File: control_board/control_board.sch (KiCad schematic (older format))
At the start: 38 parts, among them J1 Conn_01x08_Male, K1 G5Q-1A, Q1 Q_NPN_BEC, U1 MC78M05_TO252, U2 TSR_1-24120, U3 74LS02, U4 74LS02, U5 Conn_01x08_Male

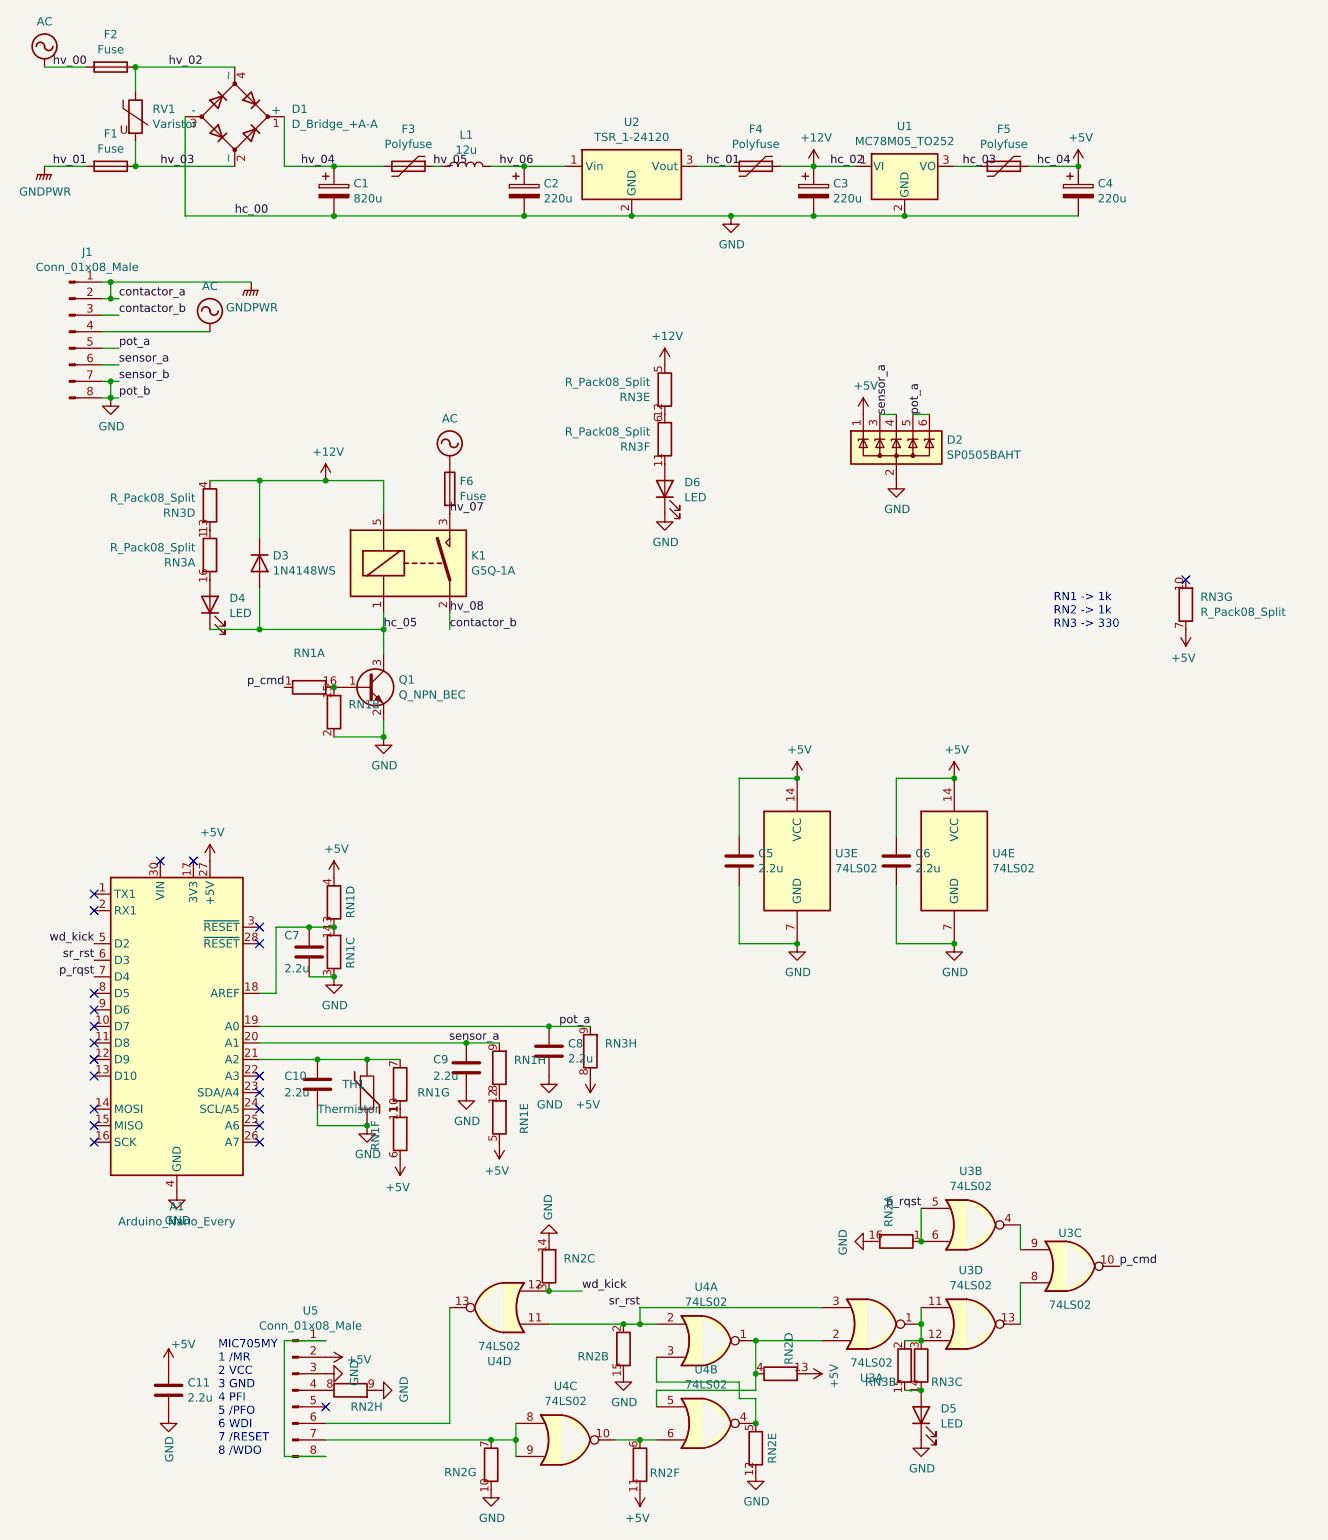
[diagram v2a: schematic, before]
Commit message: Revise schematic and some footprints
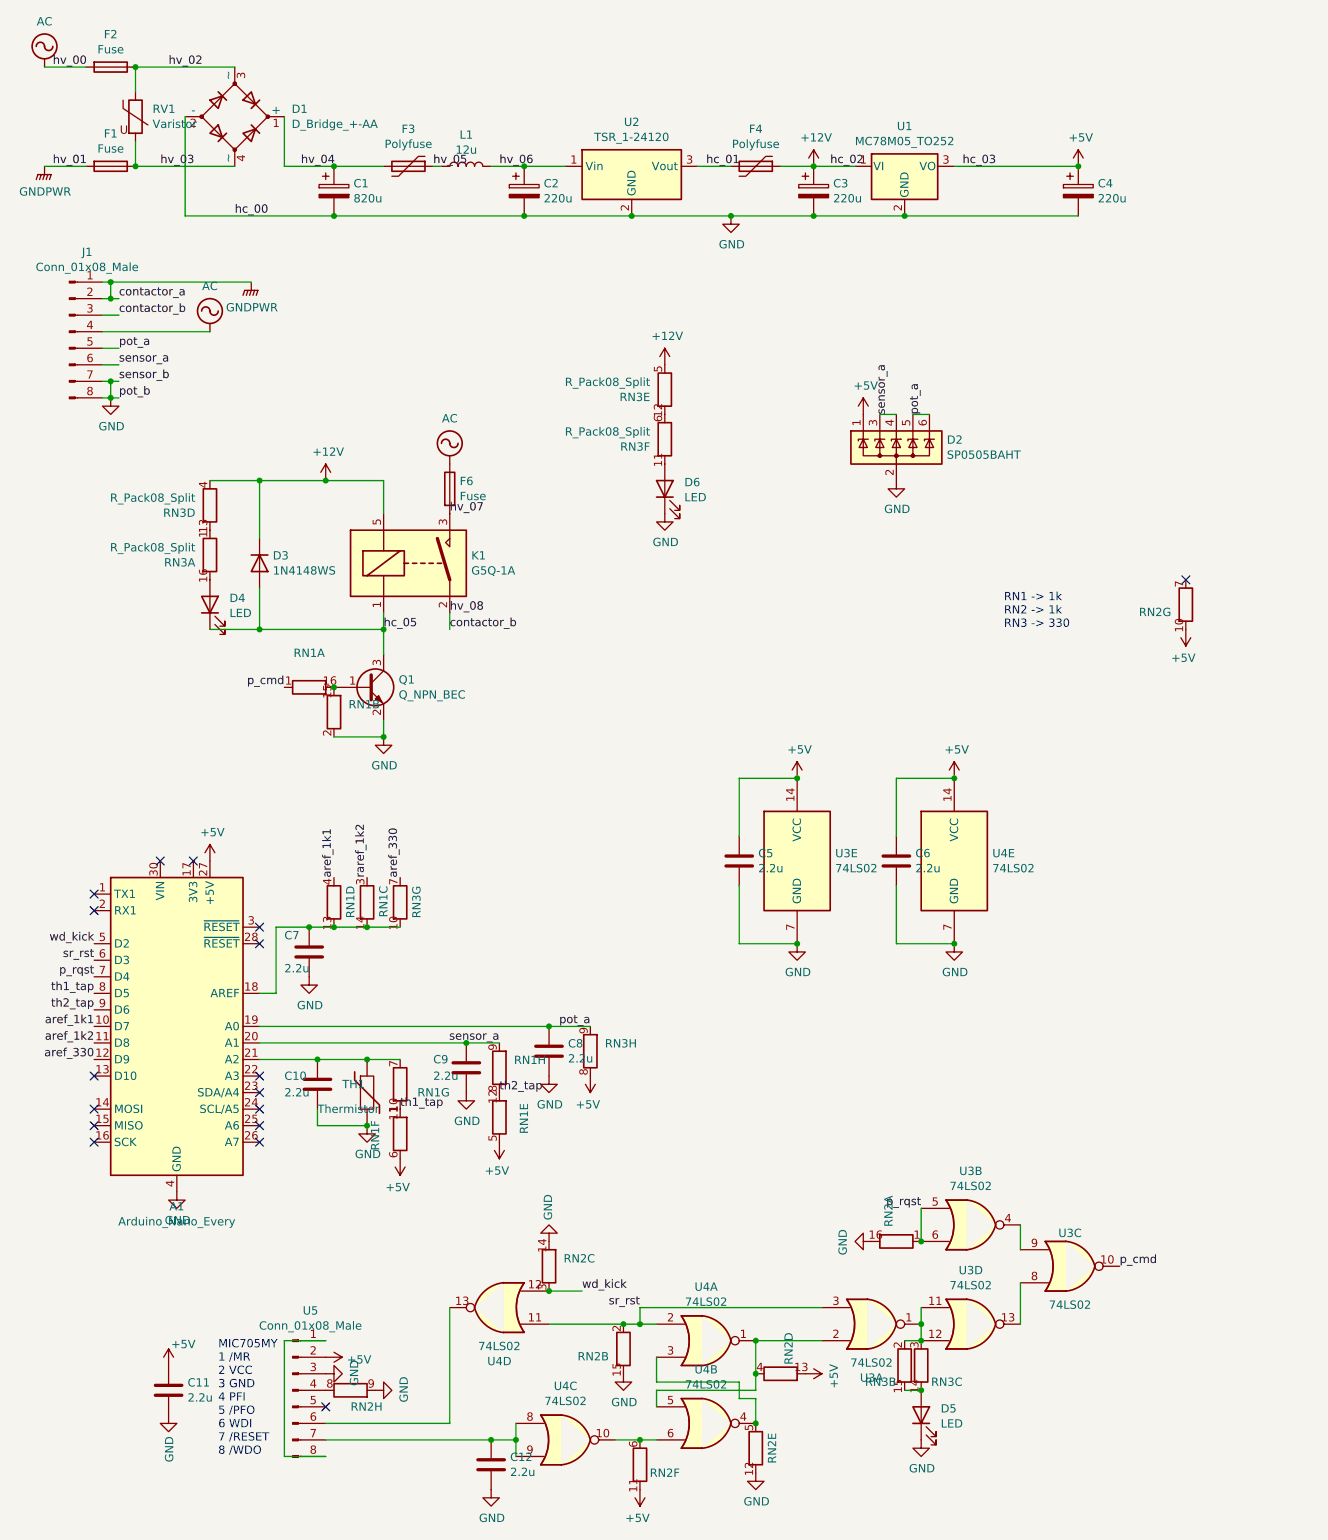
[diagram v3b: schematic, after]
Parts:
- removed D1: D_Bridge_+A-A, Diode_SMD:Diode_Bridge_Diotec_ABS, symbol Device:D_Bridge_+A-A
- removed F5: Polyfuse, Fuse:Fuse_2920_7451Metric_Pad2.10x5.45mm_HandSolder, symbol Device:Polyfuse
- added C12: 2.2u, Capacitor_SMD:C_0805_2012Metric_Pad1.18x1.45mm_HandSolder, symbol Device:C
- added D1: D_Bridge_+-AA, Diode_SMD:Diode_Bridge_Diotec_ABS, symbol Device:D_Bridge_+-AA
- F1, F2: footprint Resistor_THT:R_Axial_Power_L20.0mm_W6.4mm_P22.40mm -> Resistor_THT:R_Axial_DIN0411_L9.9mm_D3.6mm_P12.70mm_Horizontal
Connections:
- net hc_03 is gone; now on net +5V: U1.3 (VO)
- net +5V: now also RN2.10 (R7.2); no longer RN1.4 (R4.1), RN3.7 (R7.1)
- net GND: now also C12.2, D1.2 (-); no longer RN1.3 (R3.1), RN2.10 (R7.2)
- net hv_02: now also D1.3 (~~)
- net hv_03: now also D1.4 (~~)
- net hv_04: now also D1.1 (+)
- net aref_1k1: now reaches A1.10 (D7)
- net aref_1k1: now also RN1.4 (R4.1)
- net aref_1k2: now reaches A1.11 (D8)
- net aref_330: now reaches A1.12 (D9)
- net aref_330: now also RN3.7 (R7.1)
- net at A1.18 (AREF), C7.1, RN1.13 (R4.2)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: now also RN3.10 (R7.2)
- net th1_tap: now reaches A1.8 (D5)
- net th1_tap: now also RN1.10 (R7.2), RN1.11 (R6.2)
- net th2_tap: now reaches A1.9 (D6)
- net th2_tap: now also RN1.12 (R5.2), RN1.8 (R8.1)
- net at U4.8, U4.9, U5.7 (Pin_7): now also C12.1; no longer RN2.7 (R7.1)
- new net raref_1k2: RN1.3 (R3.1)
- no-connect marks 22 -> 17
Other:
- moved on the sheet: RN1C, RN2G, RN3G
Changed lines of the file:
@@
 F 0 "F1" V 903 1850 50  0000 C CNN
 F 1 "Fuse" V 994 1850 50  0000 C CNN
-F 2 "Resistor_THT:R_Axial_Power_L20.0mm_W6.4mm_P22.40mm" V 1030 1850 50  0001 C CNN
+F 2 "Resistor_THT:R_Axial_DIN0411_L9.9mm_D3.6mm_P12.70mm_Horizontal" V 1030 1850 50  0001 C CNN
 F 3 "~" H 1100 1850 50  0001 C CNN
 	1    1100 1850
@@
 F 0 "F2" V 903 1250 50  0000 C CNN
 F 1 "Fuse" V 994 1250 50  0000 C CNN
-F 2 "Resistor_THT:R_Axial_Power_L20.0mm_W6.4mm_P22.40mm" V 1030 1250 50  0001 C CNN
+F 2 "Resistor_THT:R_Axial_DIN0411_L9.9mm_D3.6mm_P12.70mm_Horizontal" V 1030 1250 50  0001 C CNN
 F 3 "~" H 1100 1250 50  0001 C CNN
 	1    1100 1250
@@
 	0    1    1    0
 $EndComp
-$Comp
-L Device:Polyfuse F5
-U 1 1 600316F0
-P 6500 1850
-F 0 "F5" V 6725 1850 50  0000 C CNN
-F 1 "Polyfuse" V 6634 1850 50  0000 C CNN
-F 2 "Fuse:Fuse_2920_7451Metric_Pad2.10x5.45mm_HandSolder" H 6550 1650 50  0001 L CNN
-F 3 "~" H 6500 1850 50  0001 C CNN
-	1    6500 1850
-	0    -1   -1   0
-$EndComp
 Wire Wire Line
 	4650 1850 4850 1850
@@
 	5900 2150 6950 2150
 Connection ~ 5900 2150
-Wire Wire Line
-	6650 1850 6950 1850
-Wire Wire Line
-	6200 1850 6350 1850
 $Comp
 L power:+12V #PWR03
@@
 	1700 4650 2000 4650
 Connection ~ 2000 4650
-$Comp
-L Device:D_Bridge_+A-A D1
-U 1 1 60134750
-P 1850 1550
-F 0 "D1" H 2194 1596 50  0000 L CNN
-F 1 "D_Bridge_+A-A" H 2194 1505 50  0000 L CNN
-F 2 "Diode_SMD:Diode_Bridge_Diotec_ABS" H 1850 1550 50  0001 C CNN
-F 3 "~" H 1850 1550 50  0001 C CNN
-	1    1850 1550
-	1    0    0    -1
-$EndComp
 $Comp
 L 74xx:74LS02 U4
@@
 NoConn ~ 1000 7550
 NoConn ~ 1000 7350
-NoConn ~ 1000 7250
-NoConn ~ 1000 7150
-NoConn ~ 1000 7050
-NoConn ~ 1000 6950
-NoConn ~ 1000 6850
 $Comp
 L power:GND #PWR035
@@
 L power:GND #PWR020
 U 1 1 6091E95E
-P 2450 6750
-F 0 "#PWR020" H 2450 6500 50  0001 C CNN
-F 1 "GND" H 2455 6577 50  0000 C CNN
-F 2 "" H 2450 6750 50  0001 C CNN
-F 3 "" H 2450 6750 50  0001 C CNN
-	1    2450 6750
-	1    0    0    -1
-$EndComp
-$Comp
-L power:+5V #PWR017
-U 1 1 6091EFD9
-P 2450 6150
-F 0 "#PWR017" H 2450 6000 50  0001 C CNN
-F 1 "+5V" H 2465 6323 50  0000 C CNN
-F 2 "" H 2450 6150 50  0001 C CNN
-F 3 "" H 2450 6150 50  0001 C CNN
-	1    2450 6150
+P 2300 6750
+F 0 "#PWR020" H 2300 6500 50  0001 C CNN
+F 1 "GND" H 2305 6577 50  0000 C CNN
+F 2 "" H 2300 6750 50  0001 C CNN
+F 3 "" H 2300 6750 50  0001 C CNN
+	1    2300 6750
 	1    0    0    -1
 $EndComp
@@
 	1    0    0    -1
 $EndComp
-Wire Wire Line
-	2450 6750 2300 6750
 Wire Wire Line
 	2300 6450 2450 6450
@@
 L Device:R_Pack08_Split RN2
 U 7 1 60C4FE74
-P 3400 9700
-F 0 "RN2" H 3488 9746 50  0000 L CNN
-F 1 "R_Pack08_Split" H 3488 9655 50  0001 L CNN
-F 2 "Package_SO:SOIC-16_4.55x10.3mm_P1.27mm" V 3320 9700 50  0001 C CNN
-F 3 "~" H 3400 9700 50  0001 C CNN
-	7    3400 9700
+P 7600 4500
+F 0 "RN2" H 7688 4546 50  0000 L CNN
+F 1 "R_Pack08_Split" H 7688 4455 50  0001 L CNN
+F 2 "Package_SO:SOIC-16_4.55x10.3mm_P1.27mm" V 7520 4500 50  0001 C CNN
+F 3 "~" H 7600 4500 50  0001 C CNN
+	7    7600 4500
 	-1   0    0    1
 $EndComp
@@
 L Device:R_Pack08_Split RN1
 U 3 1 60CA6899
-P 2450 6600
-F 0 "RN1" V 2550 6500 50  0000 L CNN
-F 1 "R_Pack08_Split" H 2538 6555 50  0001 L CNN
-F 2 "Package_SO:SOIC-16_4.55x10.3mm_P1.27mm" V 2370 6600 50  0001 C CNN
-F 3 "~" H 2450 6600 50  0001 C CNN
-	3    2450 6600
-	1    0    0    -1
+P 2650 6300
+F 0 "RN1" V 2550 6200 50  0000 L CNN
+F 1 "R_Pack08_Split" H 2738 6255 50  0001 L CNN
+F 2 "Package_SO:SOIC-16_4.55x10.3mm_P1.27mm" V 2570 6300 50  0001 C CNN
+F 3 "~" H 2650 6300 50  0001 C CNN
+	3    2650 6300
+	-1   0    0    1
 $EndComp
 $Comp
@@
 $EndComp
 NoConn ~ 7600 4350
-Text Notes 6800 4650 0    50   ~ 0
+Text Notes 6500 4650 0    50   ~ 0
 RN1 -> 1k\nRN2 -> 1k\nRN3 -> 330
 $Comp
@@
 L Device:R_Pack08_Split RN3
 U 7 1 612D28C1
-P 7600 4500
-F 0 "RN3" H 7688 4546 50  0000 L CNN
-F 1 "R_Pack08_Split" H 7688 4455 50  0000 L CNN
-F 2 "Package_SO:SOIC-16_4.55x10.3mm_P1.27mm" V 7520 4500 50  0001 C CNN
-F 3 "~" H 7600 4500 50  0001 C CNN
-	7    7600 4500
-	1    0    0    -1
+P 2850 6300
+F 0 "RN3" V 2750 6200 50  0000 L CNN
+F 1 "R_Pack08_Split" H 2938 6255 50  0001 L CNN
+F 2 "Package_SO:SOIC-16_4.55x10.3mm_P1.27mm" V 2770 6300 50  0001 C CNN
+F 3 "~" H 2850 6300 50  0001 C CNN
+	7    2850 6300
+	-1   0    0    1
 $EndComp
 $Comp
@@
 Text Label 6250 1850 0    50   ~ 0
 hc_03
-Text Label 6700 1850 0    50   ~ 0
-hc_04
 Text Label 2750 4650 0    50   ~ 0
 hc_05
@@
 Connection ~ 2450 5000
 Connection ~ 2450 6450
-Connection ~ 2450 6750
 Wire Wire Line
 	3950 8650 3750 8650
@@
 Wire Wire Line
 	3400 9550 3550 9550
+$Comp
+L Device:C C12
+U 1 1 6039BB5E
+P 3400 9700
+F 0 "C12" H 3515 9746 50  0000 L CNN
+F 1 "2.2u" H 3515 9655 50  0000 L CNN
+F 2 "Capacitor_SMD:C_0805_2012Metric_Pad1.18x1.45mm_HandSolder" H 3438 9550 50  0001 C CNN
+F 3 "~" H 3400 9700 50  0001 C CNN
+	1    3400 9700
+	1    0    0    -1
+$EndComp
+Wire Wire Line
+	6200 1850 6950 1850
+Text Label 1000 6850 2    50   ~ 0
+th1_tap
+Text Label 1000 6950 2    50   ~ 0
+th2_tap
+Text Label 3450 7450 0    50   ~ 0
+th2_tap
+Text Label 2850 7550 0    50   ~ 0
+th1_tap
+Text Label 2450 6150 1    50   ~ 0
+aref_1k1
+Wire Wire Line
+	2650 6450 2450 6450
+Text Label 2850 6150 1    50   ~ 0
+aref_330
+Text Label 1000 7250 2    50   ~ 0
+aref_330
+Text Label 1000 7150 2    50   ~ 0
+aref_1k2
+Text Label 1000 7050 2    50   ~ 0
+aref_1k1
+Text Label 2650 6150 1    50   ~ 0
+raref_1k2
+Wire Wire Line
+	2650 6450 2850 6450
+Connection ~ 2650 6450
+$Comp
+L Device:D_Bridge_+-AA D1
+U 1 1 604BA286
+P 1850 1550
+F 0 "D1" H 2194 1596 50  0000 L CNN
+F 1 "D_Bridge_+-AA" H 2194 1505 50  0000 L CNN
+F 2 "Diode_SMD:Diode_Bridge_Diotec_ABS" H 1850 1550 50  0001 C CNN
+F 3 "~" H 1850 1550 50  0001 C CNN
+	1    1850 1550
+	1    0    0    -1
+$EndComp
 $EndSCHEMATC

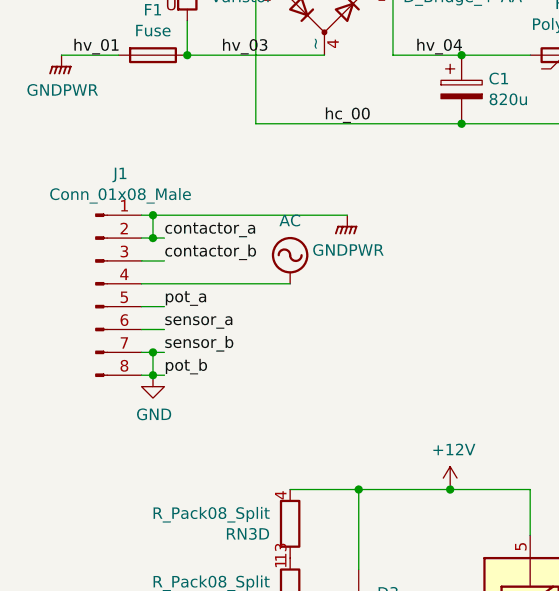
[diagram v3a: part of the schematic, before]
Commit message: Round PCB corners
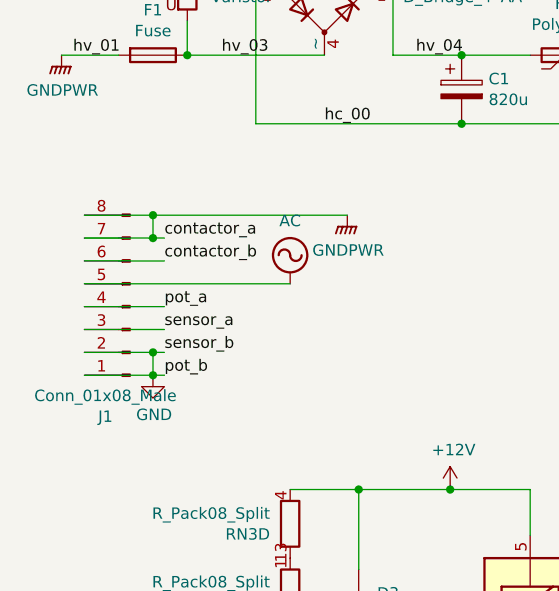
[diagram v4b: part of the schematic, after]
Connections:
- net AC: now also J1.5 (Pin_5); no longer J1.4 (Pin_4)
- net GND: now also J1.1 (Pin_1), J1.2 (Pin_2); no longer J1.7 (Pin_7), J1.8 (Pin_8)
- net GNDPWR: now also J1.7 (Pin_7), J1.8 (Pin_8); no longer J1.1 (Pin_1), J1.2 (Pin_2)
- net contactor_b: now also J1.6 (Pin_6); no longer J1.3 (Pin_3)
- net pot_a: now also J1.4 (Pin_4); no longer J1.5 (Pin_5)
- net sensor_a: now also J1.3 (Pin_3); no longer J1.6 (Pin_6)
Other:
- moved on the sheet: J1
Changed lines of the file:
@@
 L Connector:Conn_01x08_Male J1
 U 1 1 60073D15
-P 850 2850
-F 0 "J1" H 958 3331 50  0000 C CNN
-F 1 "Conn_01x08_Male" H 958 3240 50  0000 C CNN
-F 2 "Connector_JST:JST_VH_B8P-VH_1x08_P3.96mm_Vertical" H 850 2850 50  0001 C CNN
-F 3 "~" H 850 2850 50  0001 C CNN
-	1    850  2850
-	1    0    0    -1
+P 1000 2950
+F 0 "J1" H 1108 3431 50  0000 C CNN
+F 1 "Conn_01x08_Male" H 1108 3340 50  0000 C CNN
+F 2 "Connector_JST:JST_VH_B8P-VH_1x08_P3.96mm_Vertical" H 1000 2950 50  0001 C CNN
+F 3 "~" H 1000 2950 50  0001 C CNN
+	1    1000 2950
+	-1   0    0    1
 $EndComp
 $Comp
@@
 	1    0    0    -1
 $EndComp
-Wire Wire Line
-	1050 2550 1100 2550
-Wire Wire Line
-	1050 2650 1100 2650
-Wire Wire Line
-	1050 2750 1150 2750
-Wire Wire Line
-	1050 2850 1700 2850
 Text Label 1150 2950 0    50   ~ 0
 pot_a
@@
 Text Label 1150 3150 0    50   ~ 0
 sensor_b
-Wire Wire Line
-	1050 2950 1150 2950
-Wire Wire Line
-	1050 3050 1150 3050
-Wire Wire Line
-	1050 3150 1100 3150
-Wire Wire Line
-	1050 3250 1100 3250
 Text Label 3150 4650 0    50   ~ 0
 contactor_b
@@
 	1    0    0    -1
 $EndComp
+Wire Wire Line
+	800  3250 1100 3250
+Wire Wire Line
+	800  3150 1100 3150
+Wire Wire Line
+	800  3050 1150 3050
+Wire Wire Line
+	800  2950 1150 2950
+Wire Wire Line
+	800  2850 1700 2850
+Wire Wire Line
+	800  2750 1150 2750
+Wire Wire Line
+	800  2650 1100 2650
+Wire Wire Line
+	800  2550 1100 2550
 $EndSCHEMATC

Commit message: Draft layout
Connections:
- net hv_02: now also F1.1, RV1.2; no longer F2.1, RV1.1
- net hv_03: now also F2.1, RV1.1; no longer F1.1, RV1.2
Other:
- moved on the sheet: F1, F2, RV1
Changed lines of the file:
@@
 L Device:Fuse F1
 U 1 1 5FFD1BEA
+P 1100 1250
+F 0 "F1" V 903 1250 50  0000 C CNN
+F 1 "Fuse" V 994 1250 50  0000 C CNN
+F 2 "Resistor_THT:R_Axial_DIN0411_L9.9mm_D3.6mm_P12.70mm_Horizontal" V 1030 1250 50  0001 C CNN
+F 3 "~" H 1100 1250 50  0001 C CNN
+	1    1100 1250
+	0    1    1    0
+$EndComp
+$Comp
+L Device:Fuse F2
+U 1 1 5FFD1F73
 P 1100 1850
-F 0 "F1" V 903 1850 50  0000 C CNN
+F 0 "F2" V 903 1850 50  0000 C CNN
 F 1 "Fuse" V 994 1850 50  0000 C CNN
 F 2 "Resistor_THT:R_Axial_DIN0411_L9.9mm_D3.6mm_P12.70mm_Horizontal" V 1030 1850 50  0001 C CNN
 F 3 "~" H 1100 1850 50  0001 C CNN
 	1    1100 1850
-	0    1    1    0
-$EndComp
-$Comp
-L Device:Fuse F2
-U 1 1 5FFD1F73
-P 1100 1250
-F 0 "F2" V 903 1250 50  0000 C CNN
-F 1 "Fuse" V 994 1250 50  0000 C CNN
-F 2 "Resistor_THT:R_Axial_DIN0411_L9.9mm_D3.6mm_P12.70mm_Horizontal" V 1030 1250 50  0001 C CNN
-F 3 "~" H 1100 1250 50  0001 C CNN
-	1    1100 1250
 	0    1    1    0
 $EndComp
@@
 F 3 "~" H 1250 1550 50  0001 C CNN
 	1    1250 1550
-	1    0    0    -1
+	-1   0    0    1
 $EndComp
 $Comp
@@
 	1250 1700 1250 1850
 Wire Wire Line
-	1250 1850 1850 1850
-Connection ~ 1250 1850
-Wire Wire Line
-	1250 1250 1850 1250
-Connection ~ 1250 1250
-Wire Wire Line
 	950  1250 700  1250
 Wire Wire Line
@@
 L power:GNDPWR #PWR02
 U 1 1 6006AC2C
-P 700 1850
-F 0 "#PWR02" H 700 1650 50  0001 C CNN
-F 1 "GNDPWR" H 704 1696 50  0000 C CNN
-F 2 "" H 700 1800 50  0001 C CNN
-F 3 "" H 700 1800 50  0001 C CNN
-	1    700  1850
+P 700 1250
+F 0 "#PWR02" H 700 1050 50  0001 C CNN
+F 1 "GNDPWR" H 704 1096 50  0000 C CNN
+F 2 "" H 700 1200 50  0001 C CNN
+F 3 "" H 700 1200 50  0001 C CNN
+	1    700  1250
 	1    0    0    -1
 $EndComp
@@
 L power:AC #PWR01
 U 1 1 6006B79F
-P 700 1250
-F 0 "#PWR01" H 700 1150 50  0001 C CNN
-F 1 "AC" H 700 1525 50  0000 C CNN
-F 2 "" H 700 1250 50  0001 C CNN
-F 3 "" H 700 1250 50  0001 C CNN
-	1    700  1250
+P 700 1850
+F 0 "#PWR01" H 700 1750 50  0001 C CNN
+F 1 "AC" H 700 2125 50  0000 C CNN
+F 2 "" H 700 1850 50  0001 C CNN
+F 3 "" H 700 1850 50  0001 C CNN
+	1    700  1850
 	1    0    0    -1
 $EndComp
@@
 Text Label 750  1250 0    50   ~ 0
 hv_00
-Text Label 1450 1250 0    50   ~ 0
-hv_02
 Text Label 750  1850 0    50   ~ 0
 hv_01
-Text Label 1400 1850 0    50   ~ 0
-hv_03
 Text Label 2250 1850 0    50   ~ 0
 hv_04
@@
 Wire Wire Line
 	800  2550 1100 2550
+Text Label 1300 1850 0    50   ~ 0
+hv_03
+Text Label 1300 1250 0    50   ~ 0
+hv_02
+Connection ~ 1250 1850
+Wire Wire Line
+	1250 1850 1850 1850
+Connection ~ 1250 1250
+Wire Wire Line
+	1250 1250 1850 1250
 $EndSCHEMATC
